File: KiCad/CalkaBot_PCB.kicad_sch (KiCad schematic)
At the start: 6 parts, among them J1 Conn_01x03_Pin

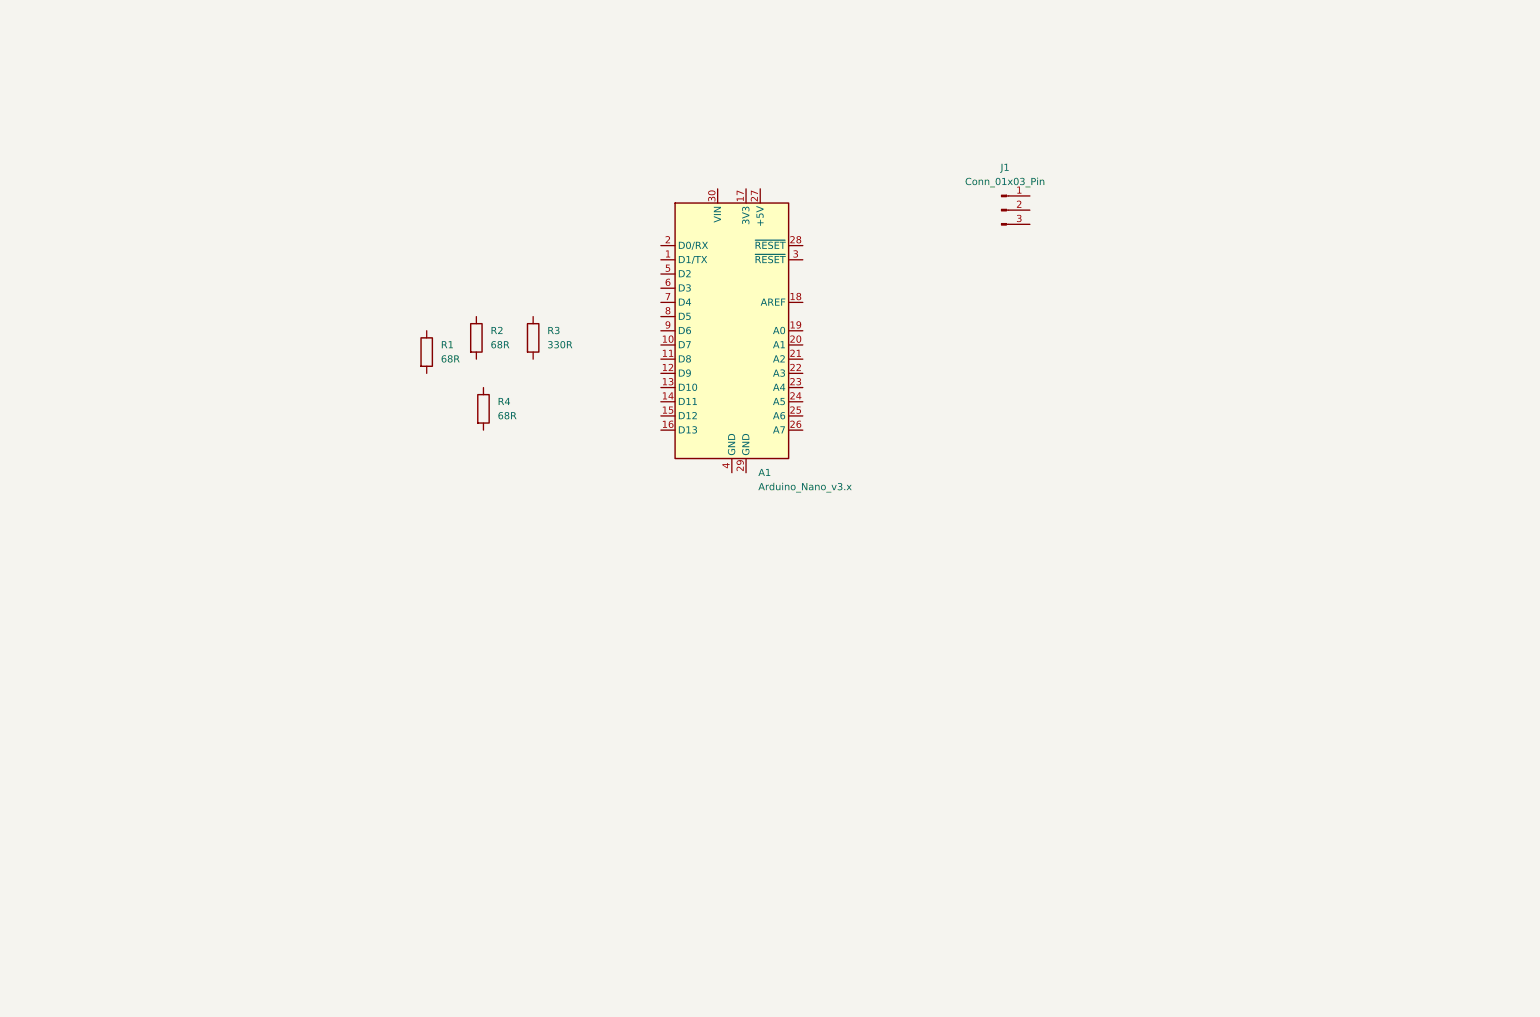
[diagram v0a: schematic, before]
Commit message: working on screws and holes on pcb
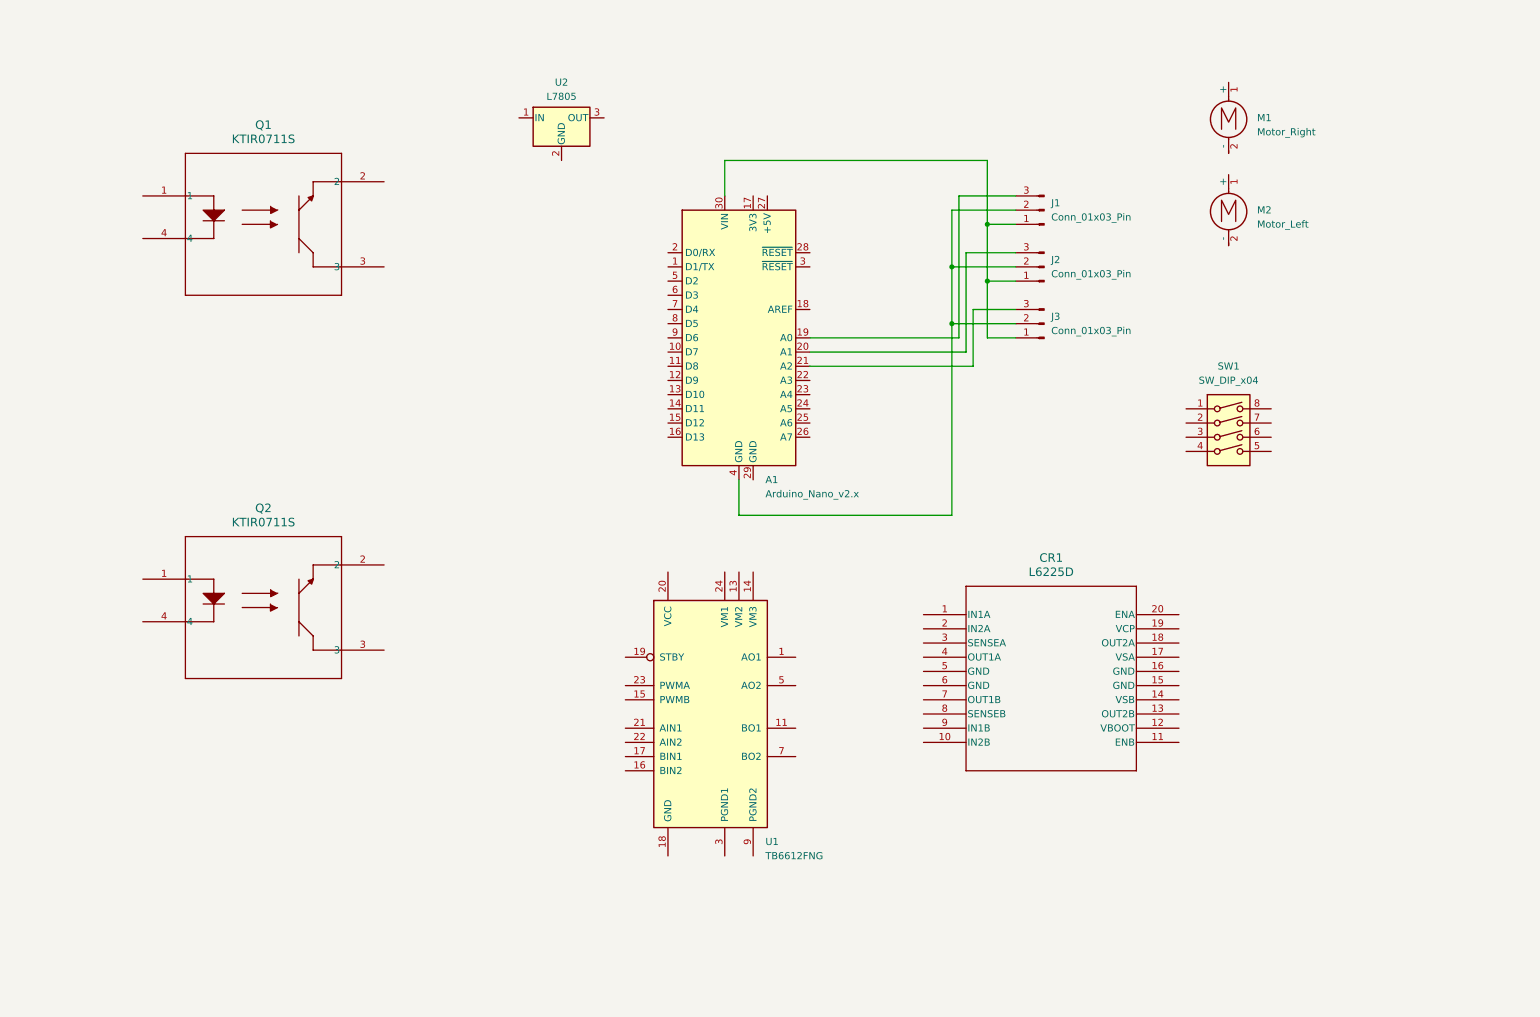
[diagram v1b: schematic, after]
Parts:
- removed A1: Arduino_Nano_v3.x, Module:Arduino_Nano, symbol MCU_Module:Arduino_Nano_v3.x
- removed R1, R2, R4: 68R, Resistor_THT:R_Axial_DIN0207_L6.3mm_D2.5mm_P7.62mm_Horizontal, symbol Device:R
- removed R3: 330R, Resistor_THT:R_Axial_DIN0207_L6.3mm_D2.5mm_P7.62mm_Horizontal, symbol Device:R
- added A1: Arduino_Nano_v2.x, Module:Arduino_Nano, symbol MCU_Module:Arduino_Nano_v2.x
- added CR1: L6225D, SO-20_STM, symbol L6225D:L6225D
- added J2, J3: Conn_01x03_Pin, Connector_JST:JST_PH_B3B-PH-K_1x03_P2.00mm_Vertical, symbol Connector:Conn_01x03_Pin
- added M1: Motor_Right, CalkaBot3k0:CalkBot3k0_Motor_Right, symbol Motor:Motor_DC
- added M2: Motor_Left, CalkaBot3k0:CalkBot3k0_Motor_Left, symbol Motor:Motor_DC
- added Q1, Q2: KTIR0711S, footprints:KTIR0711S_KNB, symbol KTIR0711S:KTIR0711S
- added SW1: SW_DIP_x04, Button_Switch_THT:SW_DIP_SPSTx04_Slide_9.78x12.34mm_W7.62mm_P2.54mm, symbol Switch:SW_DIP_x04
- added U1: TB6612FNG, Package_SO:SSOP-24_5.3x8.2mm_P0.65mm, symbol Driver_Motor:TB6612FNG
- added U2: L7805, Package_TO_SOT_THT:TO-220-3_Horizontal_TabDown, symbol Regulator_Linear:L7805
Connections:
- net at J1.1 (Pin_1): now also A1.30 (VIN), J2.1 (Pin_1), J3.1 (Pin_1)
- net at J1.2 (Pin_2): now also A1.4 (GND), J2.2 (Pin_2), J3.2 (Pin_2)
- net at J1.3 (Pin_3): now also A1.19 (A0)
- new net: A1.20 (A1), J2.3 (Pin_3)
- new net: A1.21 (A2), J3.3 (Pin_3)
- new net: U1.1 (AO1), U1.2 (AO1)
- new net: U1.10 (PGND2), U1.9 (PGND2)
- new net: U1.11 (BO1), U1.12 (BO1)
- new net: U1.3 (PGND1), U1.4 (PGND1)
- new net: U1.5 (AO2), U1.6 (AO2)
- new net: U1.7 (BO2), U1.8 (BO2)
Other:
- moved on the sheet: J1

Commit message: working on PCB + changes within NX for project review
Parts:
- removed U1: TB6612FNG, Package_SO:SSOP-24_5.3x8.2mm_P0.65mm, symbol Driver_Motor:TB6612FNG
- removed U2: L7805, Package_TO_SOT_THT:TO-220-3_Horizontal_TabDown, symbol Regulator_Linear:L7805
- added C1, C2: C, symbol Device:C
- added J4: Conn_01x02_Pin, Connector_PinSocket_1.00mm:PinSocket_1x02_P1.00mm_Vertical, symbol Connector:Conn_01x02_Pin
- added R1, R3: 20k, Resistor_SMD:R_0805_2012Metric_Pad1.20x1.40mm_HandSolder, symbol Device:R
- added R4, R5: 220, Resistor_SMD:R_0805_2012Metric_Pad1.20x1.40mm_HandSolder, symbol Device:R
- added U1: L78M05CDT-TR, L78M05CDT-TR:VREG_L78M05CDT-TR, symbol L78M05CDT-TR:L78M05CDT-TR
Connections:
- net at Q1.1: now also R4.1
- net at Q1.2: now also A1.23 (A4), R1.1
- net GND: now reaches Q1.3
- net GND: now also A1.4 (GND), J1.2 (Pin_2), J2.2 (Pin_2), J3.2 (Pin_2), Q1.4, Q2.3, Q2.4, C1.2, C2.2, J4.2 (Pin_2), U1.2 (GND)
- net +5V: now reaches A1.30 (VIN), J1.1 (Pin_1), J2.1 (Pin_1), J3.1 (Pin_1)
- net +5V: now also C2.1, R1.2, R3.2, R4.2, R5.2, U1.3 (OUT)
- net at Q2.1: now also R5.1
- net at Q2.2: now also A1.22 (A3), R3.1
- new net +7.5V: C1.1, J4.1 (Pin_1), U1.1 (IN)
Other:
- moved on the sheet: A1, CR1, J1, J2, J3, M1, M2, Q1, Q2, SW1

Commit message: w trakcie ukladania elementow
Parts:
- added C11, C12, C7, C9: 0u1, Capacitor_SMD:C_0805_2012Metric_Pad1.18x1.45mm_HandSolder, symbol Device:C
- added C3: 10n, Capacitor_SMD:C_0805_2012Metric_Pad1.18x1.45mm_HandSolder, symbol Device:C
- added C4: 200n, Capacitor_SMD:C_0805_2012Metric_Pad1.18x1.45mm_HandSolder, symbol Device:C
- added C5, C6: 5n6, Capacitor_SMD:C_0805_2012Metric_Pad1.18x1.45mm_HandSolder, symbol Device:C
- added C8: 100u, Capacitor_SMD:CP_Elec_8x10.5, symbol Device:C_Polarized
- added D1, D2: 1N4148WT, Diode_SMD:D_SOD-523, symbol Diode:1N4148WT
- added D3: SS14, Diode_SMD:D_SMA_Handsoldering, symbol Device:D
- added J5: MOTOR3, Connector_PinHeader_2.54mm:PinHeader_1x02_P2.54mm_Vertical, symbol Connector:Conn_01x02_Pin
- added J6: StartModule, Connector_PinHeader_2.54mm:PinHeader_1x03_P2.54mm_Vertical, symbol Connector:Conn_01x03_Pin
- added Q3: IRLL014NTRPBF, Package_TO_SOT_SMD:SOT-223, symbol Transistor_BJT:BC107
- added R2: 100R, Resistor_SMD:R_0805_2012Metric_Pad1.20x1.40mm_HandSolder, symbol Device:R
- added R6, R7: 100k, Resistor_SMD:R_0805_2012Metric_Pad1.20x1.40mm_HandSolder, symbol Device:R
- C1: value C -> 0u33; footprint (none) -> Capacitor_SMD:C_0805_2012Metric_Pad1.18x1.45mm_HandSolder
- C2: value C -> 0u1; footprint (none) -> Capacitor_SMD:C_0805_2012Metric_Pad1.18x1.45mm_HandSolder
- CR1: value L6225D -> L6225PD; footprint SO-20_STM -> Package_SO:SO-20-1EP_7.52x12.825mm_P1.27mm_EP6.045x12.09mm_Mask3.56x4.47mm_ThermalVias
- J4: footprint Connector_PinSocket_1.00mm:PinSocket_1x02_P1.00mm_Vertical -> Connector_PinHeader_2.54mm:PinHeader_1x02_P2.54mm_Vertical
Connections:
- net +5V: now also J6.1 (Pin_1)
- net +7.5V: now also CR1.19 (VSB), CR1.2 (VSA), C4.1, C7.1, C8.1, C9.1, D1.2 (A), Q3.3 (C)
- net GND: now also A1.29 (GND), CR1.1 (GND), CR1.10 (GND), CR1.11 (GND), CR1.13 (SENSEB), CR1.20 (GND), CR1.8 (SENSEA), SW1.1, SW1.2, SW1.3, SW1.4, C5.1, C6.1, C7.2, C8.2, C9.2, D3.2 (A), J5.1 (Pin_1), J6.2 (Pin_2)
- net FLOOR_SENSOR_LEFT: now reaches A1.23 (A4), Q1.2, R1.1
- net at CR1.12 (OUT1B): now also M2.1 (+), C12.2
- net M_IN1B: now reaches CR1.14 (IN1B)
- net M_IN1B: now also A1.14 (D11)
- net M_IN2B: now reaches CR1.15 (IN2B)
- net M_IN2B: now also A1.13 (D10)
- net at CR1.16 (ENB): now also C6.2, R7.1
- net at CR1.17 (VBOOT): now also C4.2, D2.1 (K)
- net at CR1.18 (OUT2B): now also M2.2 (-), C12.1
- net at CR1.3 (OUT2A): now also M1.1 (+), C11.2
- net at CR1.4 (VCP): now also C3.2
- net at CR1.5 (ENA): now also C5.2, R6.1
- net M_IN1A: now reaches CR1.6 (IN1A)
- net M_IN1A: now also A1.16 (D13)
- net M_IN2A: now reaches CR1.7 (IN2A)
- net M_IN2A: now also A1.15 (D12)
- net at CR1.9 (OUT1A): now also M1.2 (-), C11.1
- net FLOOR_SENSOR_RIGHT: now reaches A1.22 (A3), Q2.2, R3.1
- net M_FRONT: now reaches A1.10 (D7)
- net M_FRONT: now also Q3.2 (B)
- net M_ENB: now reaches A1.11 (D8)
- net M_ENB: now also R7.2
- net M_ENA: now reaches A1.12 (D9)
- net M_ENA: now also R6.2
- net START_MODULE: now reaches A1.9 (D6)
- net START_MODULE: now also J6.3 (Pin_3)
- new net: D1.1 (K), D2.2 (A), R2.1
- new net: D3.1 (K), J5.2 (Pin_2), Q3.1 (E)
- new net: C3.1, R2.2
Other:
- moved on the sheet: C1, C2, CR1, J1, J2, J3, J4, M1, M2, Q1, Q2, R1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

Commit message: PCB finished ready to send
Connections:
- net FLOOR_SENSOR_LEFT: now also A1.20 (A1); no longer A1.23 (A4)
- net FLOOR_SENSOR_RIGHT: now also A1.19 (A0); no longer A1.22 (A3)
- net GND: now also CR1.21 (GND)
- net M_ENA: now also A1.16 (D13); no longer A1.12 (D9)
- net M_ENB: now also A1.15 (D12); no longer A1.11 (D8)
- net M_FRONT: now also A1.6 (D3); no longer A1.10 (D7)
- net M_IN1A: now also A1.12 (D9); no longer A1.16 (D13)
- net M_IN1B: now also A1.13 (D10); no longer A1.14 (D11)
- net M_IN2A: now also A1.11 (D8); no longer A1.15 (D12)
- net M_IN2B: now also A1.14 (D11); no longer A1.13 (D10)
- net START_MODULE: now also A1.5 (D2); no longer A1.9 (D6)
- net at J1.3 (Pin_3): now also A1.23 (A4); no longer A1.19 (A0)
- net at SW1.5: now also A1.10 (D7)
- net at SW1.6: now also A1.9 (D6)
- net at SW1.7: now also A1.8 (D5)
- net at SW1.8: now also A1.7 (D4)
- net at J2.3 (Pin_3): now also A1.21 (A2); no longer A1.20 (A1)
- net at J3.3 (Pin_3): now also A1.22 (A3); no longer A1.21 (A2)
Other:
- moved on the sheet: J1, J2, J3, SW1

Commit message: płytka leci a rece sa gotowe do druku
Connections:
- no-connect marks 0 -> 10
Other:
- moved on the sheet: D1
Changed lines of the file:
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@@
 		(color 0 0 0 0)
 	)
+	(no_connect
+		(at 123.19 81.28)
+	)
+	(no_connect
+		(at 123.19 104.14)
+	)
+	(no_connect
+		(at 115.57 60.96)
+	)
+	(no_connect
+		(at 123.19 73.66)
+	)
+	(no_connect
+		(at 113.03 60.96)
+	)
+	(no_connect
+		(at 123.19 99.06)
+	)
+	(no_connect
+		(at 123.19 71.12)
+	)
+	(no_connect
+		(at 97.79 71.12)
+	)
+	(no_connect
+		(at 97.79 73.66)
+	)
+	(no_connect
+		(at 123.19 101.6)
+	)
 	(wire
 		(pts
@@
 	(wire
 		(pts
-			(xy 92.71 147.32) (xy 92.71 152.4)
+			(xy 92.71 148.59) (xy 92.71 152.4)
 		)
 		(stroke
@@
 	(wire
 		(pts
+			(xy 92.71 140.97) (xy 92.71 139.7)
+		)
+		(stroke
+			(width 0)
+			(type default)
+		)
+	)
+	(wire
+		(pts
 			(xy 35.56 105.41) (xy 44.45 105.41)
 		)
@@
 	(wire
 		(pts
+			(xy 52.07 34.29) (xy 52.07 35.56)
+		)
+		(stroke
+			(width 0)
+			(type default)
+		)
+	)
+	(wire
+		(pts
 			(xy 208.28 91.44) (xy 208.28 92.71)
 		)
@@
 	(symbol
 		(lib_id "power:+7.5V")
-		(at 52.07 35.56 0)
+		(at 52.07 34.29 0)
 		(unit 1)
 		(exclude_from_sim no)
@@
 		(fields_autoplaced yes)
 		(property "Reference" "#PWR015"
-			(at 52.07 39.37 0)
+			(at 52.07 38.1 0)
 			(effects
 				(font
@@
 		)
 		(property "Value" "+7.5V"
-			(at 52.07 30.48 0)
+			(at 52.07 29.21 0)
 			(effects
 				(font
@@
 		)
 		(property "Footprint" ""
-			(at 52.07 35.56 0)
+			(at 52.07 34.29 0)
 			(effects
 				(font
@@
 		)
 		(property "Datasheet" ""
-			(at 52.07 35.56 0)
+			(at 52.07 34.29 0)
 			(effects
 				(font
@@
 		)
 		(property "Description" "Power symbol creates a global label with name \"+7.5V\""
-			(at 52.07 35.56 0)
+			(at 52.07 34.29 0)
 			(effects
 				(font
@@
 	(symbol
 		(lib_id "Diode:1N4148WT")
-		(at 92.71 143.51 90)
+		(at 92.71 144.78 90)
 		(unit 1)
 		(exclude_from_sim no)
@@
 		(dnp no)
 		(property "Reference" "D1"
-			(at 93.98 140.97 90)
+			(at 93.98 142.24 90)
 			(effects
 				(font
@@
 		)
 		(property "Value" "1N4148WT"
-			(at 93.98 143.51 90)
+			(at 93.98 144.78 90)
 			(effects
 				(font
@@
 		)
 		(property "Footprint" "Diode_SMD:D_SOD-523"
-			(at 97.155 143.51 0)
+			(at 97.155 144.78 0)
 			(effects
 				(font
@@
 		)
 		(property "Datasheet" "https://www.diodes.com/assets/Datasheets/ds30396.pdf"
-			(at 92.71 143.51 0)
+			(at 92.71 144.78 0)
 			(effects
 				(font
@@
 		)
 		(property "Description" "75V 0.15A Fast switching Diode, SOD-523"
-			(at 92.71 143.51 0)
+			(at 92.71 144.78 0)
 			(effects
 				(font
@@
 		)
 		(property "Sim.Device" "D"
-			(at 92.71 143.51 0)
+			(at 92.71 144.78 0)
 			(effects
 				(font
@@
 		)
 		(property "Sim.Pins" "1=K 2=A"
-			(at 92.71 143.51 0)
+			(at 92.71 144.78 0)
 			(effects
 				(font

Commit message: working on soft and 2nd version of board
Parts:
- removed Q3: IRLL014NTRPBF, Package_TO_SOT_SMD:SOT-223, symbol Transistor_BJT:BC107
- added Q3: BS108, Package_TO_SOT_THT:TO-92_Inline, symbol Transistor_FET:BS108
- CR1: footprint Package_SO:SO-20-1EP_7.52x12.825mm_P1.27mm_EP6.045x12.09mm_Mask3.56x4.47mm_ThermalVias -> CalkaBot3k0:PowerSO-20
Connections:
- net +7.5V: now also Q3.3 (S)
- net M_FRONT: now also Q3.2 (G)
- net at D3.1 (K), J5.2 (Pin_2): now also Q3.1 (D)
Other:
- moved on the sheet: C9, D3, J5

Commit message: wyslano druga plytke pisze sie praca i program
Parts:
- removed C9: 0u1, Capacitor_SMD:C_0805_2012Metric_Pad1.18x1.45mm_HandSolder, symbol Device:C
- added D4: LED, LED_SMD:LED_0805_2012Metric_Pad1.15x1.40mm_HandSolder, symbol Device:LED
- added R8, R9: 10k, Resistor_SMD:R_0805_2012Metric_Pad1.20x1.40mm_HandSolder, symbol Device:R
- C8: footprint Capacitor_SMD:CP_Elec_8x10.5 -> Capacitor_SMD:CP_Elec_6.3x7.7
- CR1: footprint CalkaBot3k0:PowerSO-20 -> CalkaBot3k0:L6225PD
- Q1, Q2: footprint footprints:KTIR0711S_KNB -> CalkaBot3k0:KTIR0711S
- Q3: footprint Package_TO_SOT_THT:TO-92_Inline -> CalkaBot3k0:SOT-223-IRLL014NTRPBF
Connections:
- net +5V: now also A1.27 (+5V), R1.1, R3.1; no longer A1.30 (VIN), R1.2, R3.2
- net +7.5V: now also D3.1 (K), J5.1 (Pin_1); no longer Q3.3 (S)
- net FLOOR_SENSOR_LEFT: now also A1.19 (A0), Q1.3, R1.2; no longer A1.20 (A1), Q1.2, R1.1
- net FLOOR_SENSOR_RIGHT: now also A1.20 (A1), Q2.3, R3.2; no longer A1.19 (A0), Q2.2, R3.1
- net GND: now also Q1.2, Q2.2, Q3.3 (S), D4.1 (K), R8.2; no longer D3.2 (A), J5.1 (Pin_1), Q1.3, Q2.3
- net M_FRONT: now also R8.1
- net at J5.2 (Pin_2), Q3.1 (D): now also D3.2 (A); no longer D3.1 (K)
- net at A1.24 (A5): now also R9.1
- new net: D4.2 (A), R9.2
- no-connect marks 10 -> 9
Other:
- moved on the sheet: D3, R1, R3
